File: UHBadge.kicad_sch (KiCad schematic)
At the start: 77 parts, among them J1 Conn_01x03_MountingPin, P1 USB_C_Plug_USB2.0, Q1 Si1308EDL, SW1 Boot, SW2 Run, U1 RP2350A, U2 MCP73871, U3 W25Q128JVS, U4 SRV05-4, U5 Conn, U6 ST25DV64K-JFR6D3, Y1 12MHz

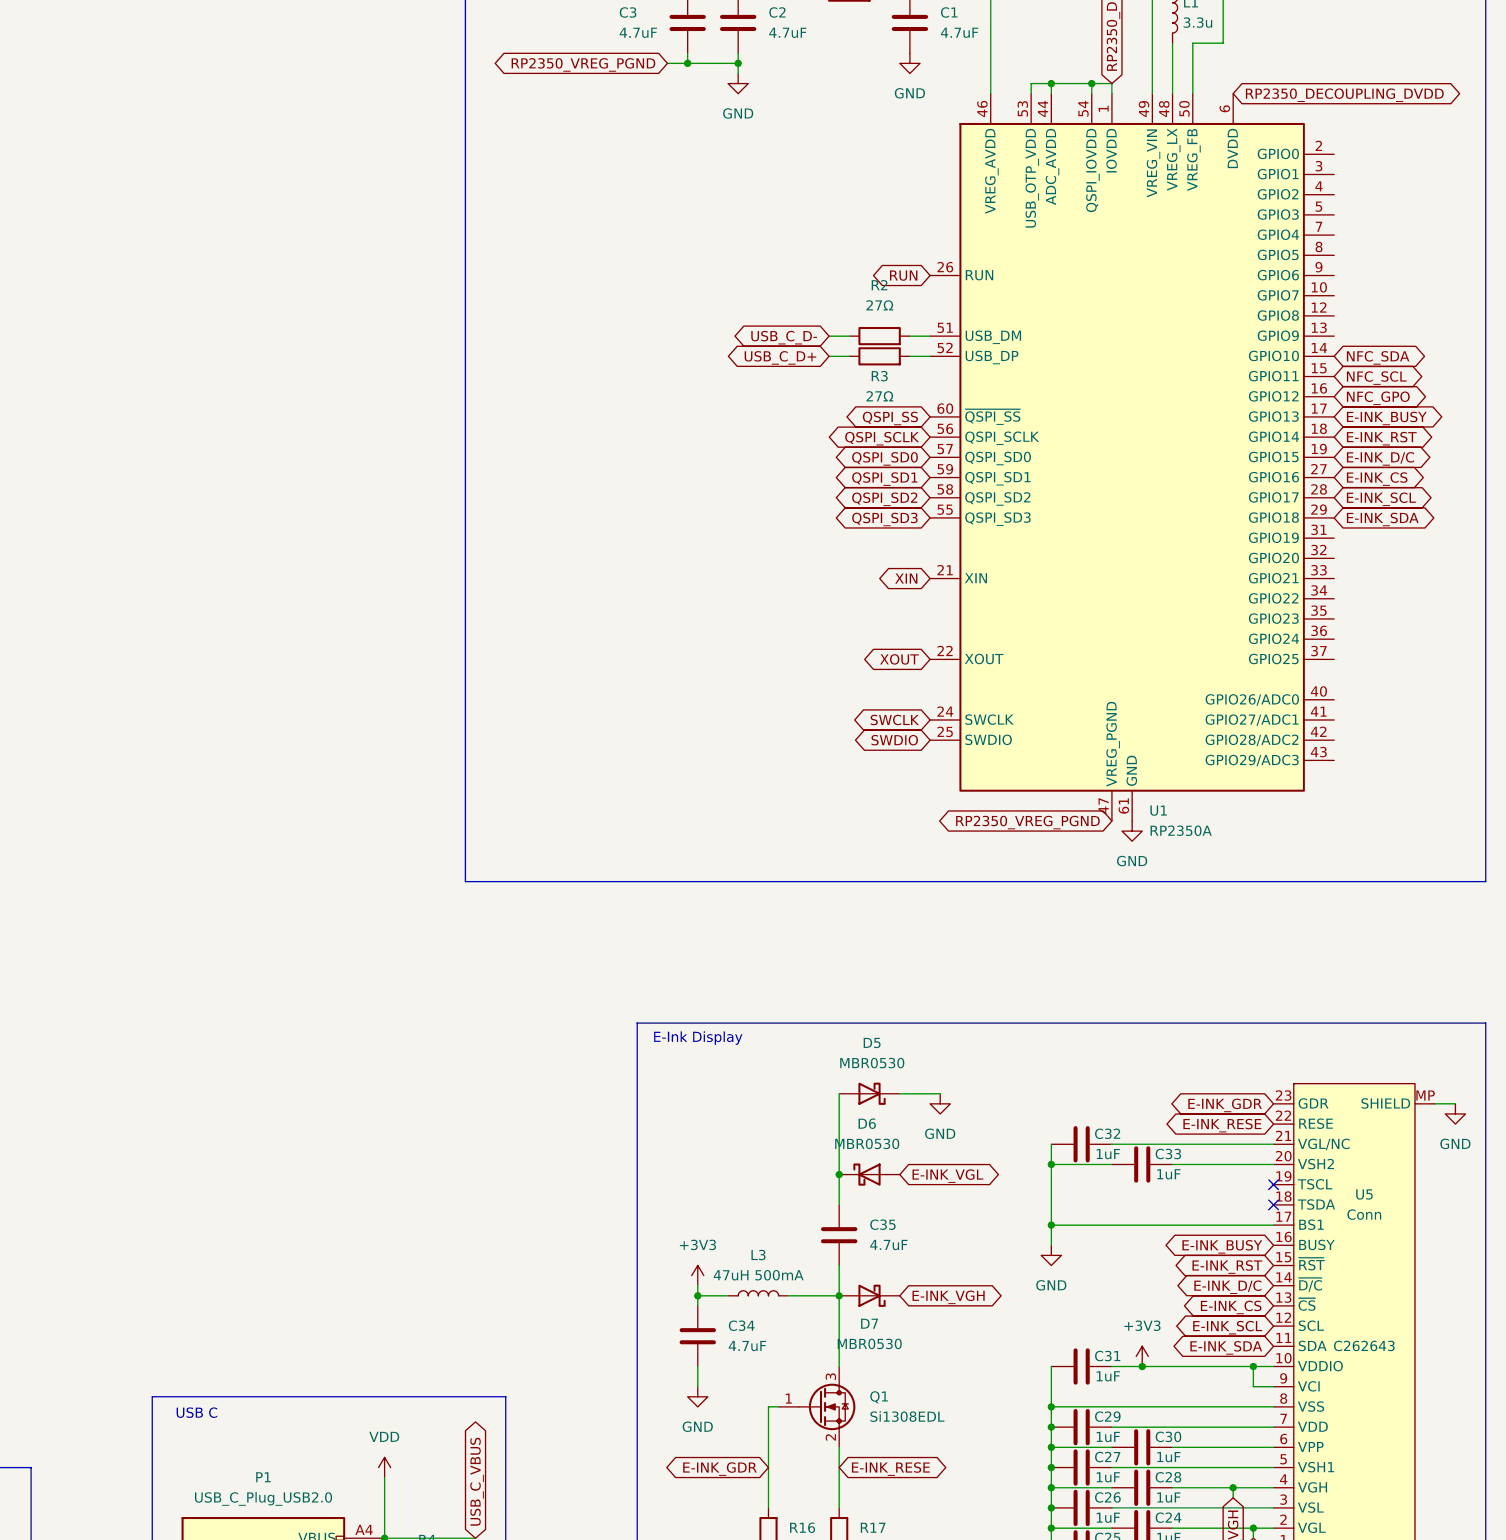
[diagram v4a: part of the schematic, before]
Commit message: Added RP2350 expansion GPIO pins.
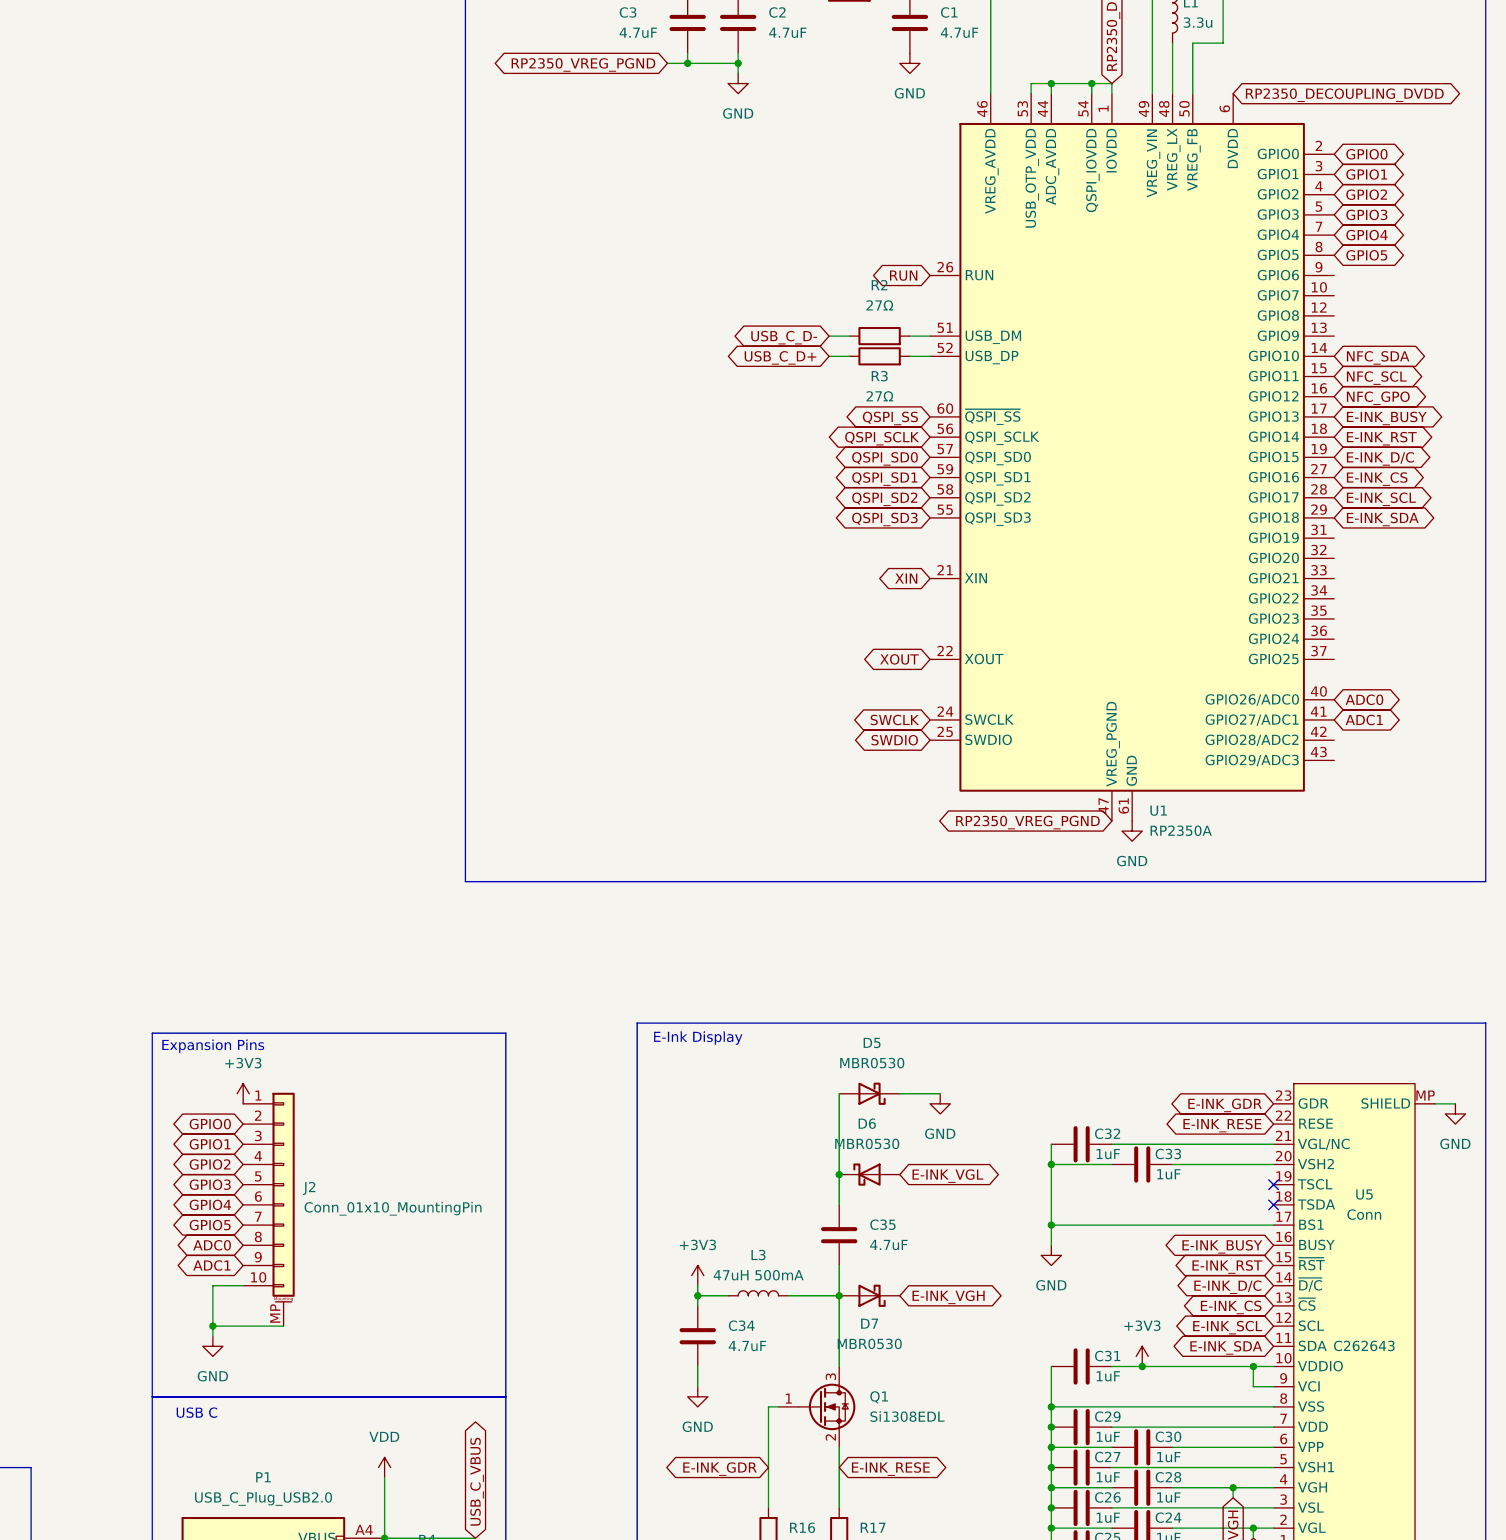
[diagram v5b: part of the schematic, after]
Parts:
- added J2: Conn_01x10_MountingPin, symbol Connector_Generic_MountingPin:Conn_01x10_MountingPin
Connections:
- net +3V3: now also J2.1 (Pin_1)
- net -BATT: now also J2.10 (Pin_10), J2.MP (MountPin)
- net GPIO0: now reaches U1.2 (GPIO0)
- net GPIO0: now also J2.2 (Pin_2)
- net GPIO1: now reaches U1.3 (GPIO1)
- net GPIO1: now also J2.3 (Pin_3)
- net GPIO2: now reaches U1.4 (GPIO2)
- net GPIO2: now also J2.4 (Pin_4)
- net ADC0: now reaches U1.40 (GPIO26/ADC0)
- net ADC0: now also J2.8 (Pin_8)
- net ADC1: now reaches U1.41 (GPIO27/ADC1)
- net ADC1: now also J2.9 (Pin_9)
- net GPIO3: now reaches U1.5 (GPIO3)
- net GPIO3: now also J2.5 (Pin_5)
- net GPIO4: now reaches U1.7 (GPIO4)
- net GPIO4: now also J2.6 (Pin_6)
- net GPIO5: now reaches U1.8 (GPIO5)
- net GPIO5: now also J2.7 (Pin_7)
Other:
- note added: "Expansion Pins"

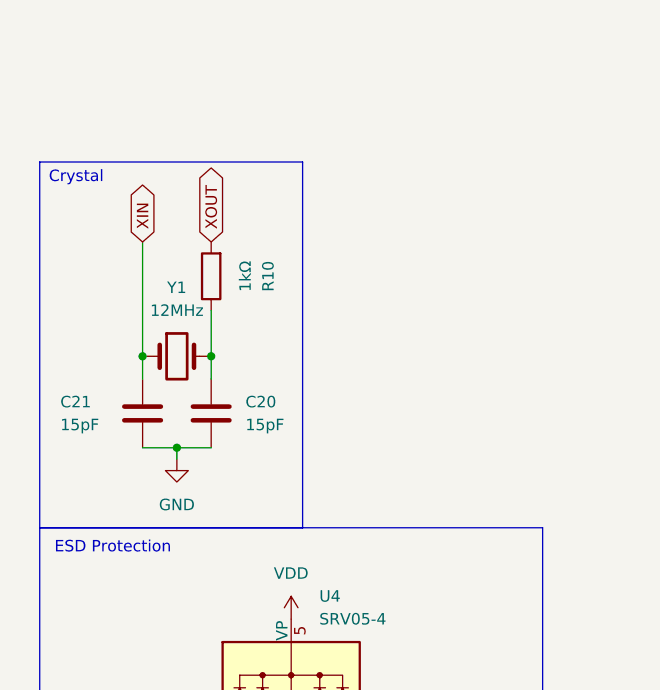
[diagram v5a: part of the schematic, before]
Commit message: Added footprints.
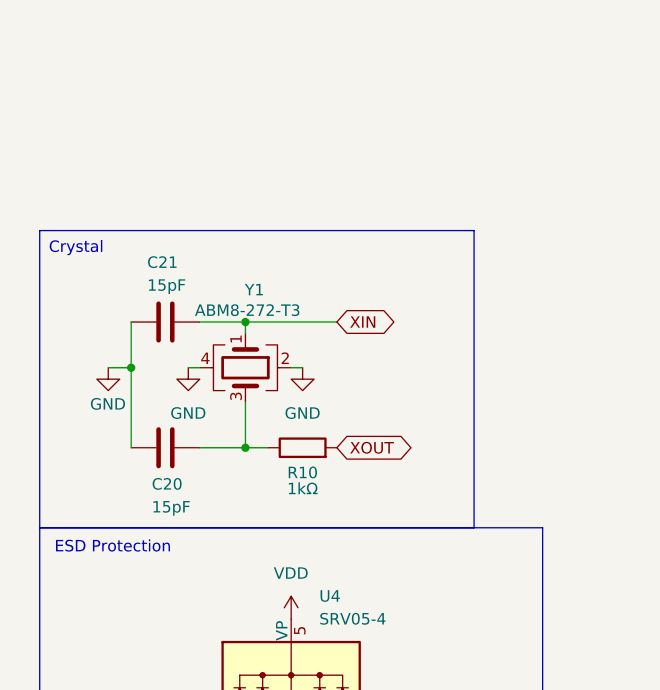
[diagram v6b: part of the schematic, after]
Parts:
- removed Y1: 12MHz, symbol Device:Crystal
- added Y1: ABM8-272-T3, Crystal:Crystal_SMD_3225-4Pin_3.2x2.5mm, symbol Device:Crystal_GND23
- C1, C10, C11, C12, C13, C14, C15, C16, C17, C18, C19, C2, C20, C21, C22, C23, C24, C25, C26, C27, C28, C29, C3, C30, C31, C32, C33, C34, C35, C4, C5, C6, C7, C8, C9: footprint (none) -> Capacitor_SMD:C_0402_1005Metric
- D1, D2, D3, D4: footprint (none) -> LED_SMD:LED_0805_2012Metric
- H1, H2: footprint (none) -> MountingHole:MountingHole_2.2mm_M2_Pad_Via
- J1: footprint (none) -> Connector_PinHeader_1.00mm:PinHeader_1x03_P1.00mm_Vertical
- J2: footprint (none) -> Connector_PinHeader_1.00mm:PinHeader_1x10_P1.00mm_Vertical
- L1: footprint (none) -> CustomFootprints:Inductor
- L2: footprint (none) -> CustomFootprints:NFC_Antenna
- L3: footprint (none) -> Inductor_SMD:L_APV_ANR4018
- P1: footprint (none) -> Connector_USB:USB_C_Receptacle_GCT_USB4105-xx-A_16P_TopMnt_Horizontal
- R1, R10, R11, R12, R13, R14, R15, R16, R17, R2, R3, R4, R5, R6, R7, R8, R9: footprint (none) -> Resistor_SMD:R_0402_1005Metric
- SW1, SW2: footprint (none) -> Button_Switch_THT:SW_PUSH-12mm_Wuerth-430476085716
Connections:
- net -BATT: now also Y1.2, Y1.4
- net XIN: now also Y1.1
- net at C20.1, R10.1: now also Y1.3
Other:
- moved on the sheet: C20, C21, R10

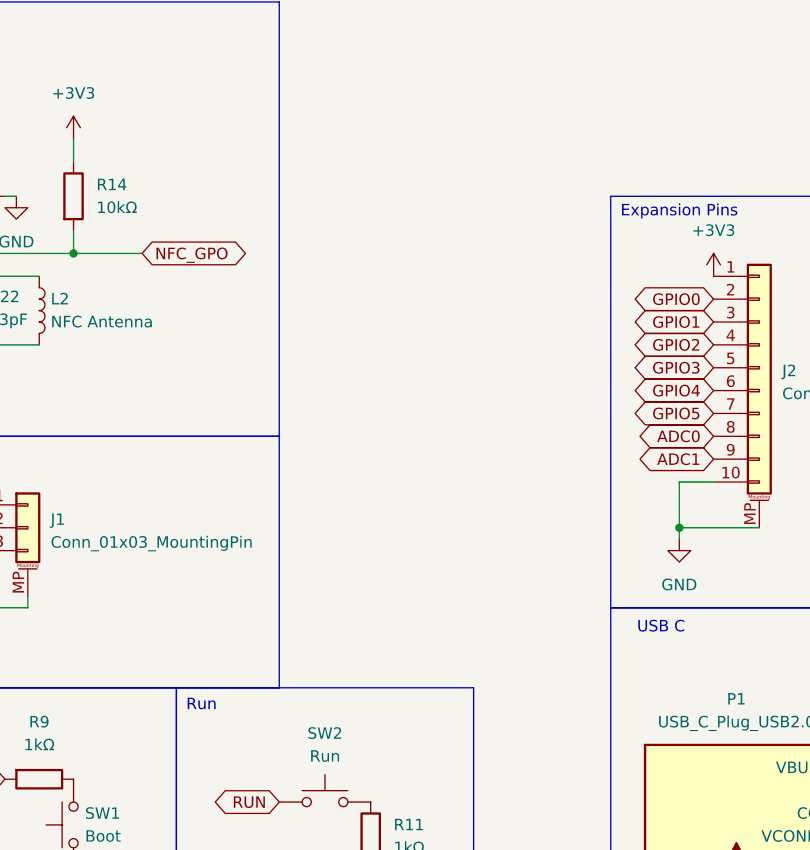
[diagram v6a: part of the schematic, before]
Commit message: Created the Badge borders. Fixed the buttons footprints.
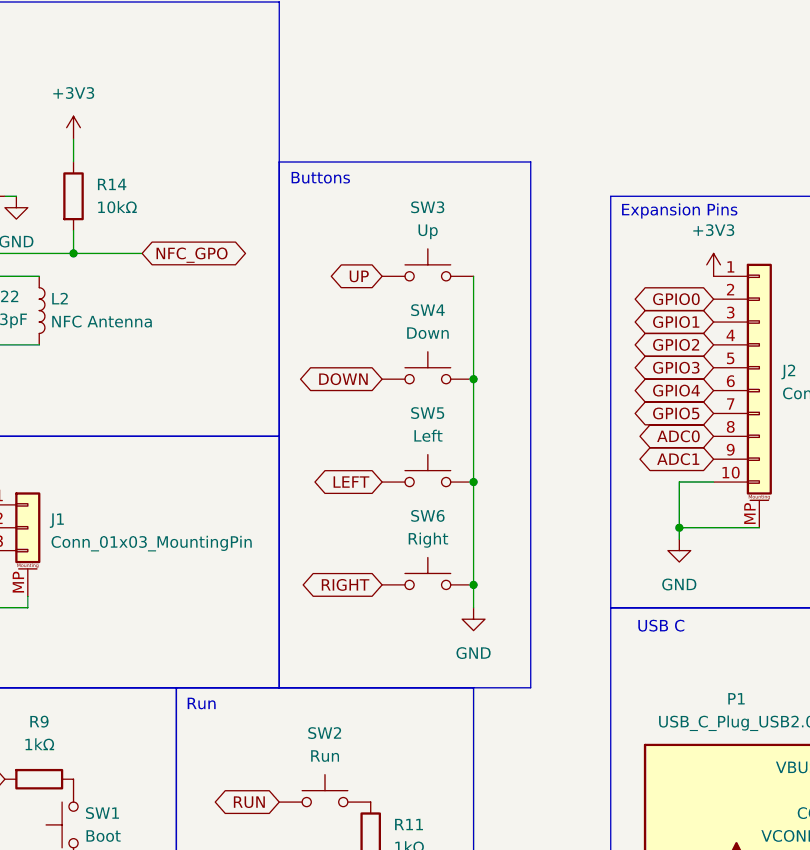
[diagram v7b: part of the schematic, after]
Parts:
- added SW3: Up, Button_Switch_THT:SW_PUSH_6mm, symbol Switch:SW_Push
- added SW4: Down, Button_Switch_THT:SW_PUSH_6mm, symbol Switch:SW_Push
- added SW5: Left, Button_Switch_THT:SW_PUSH_6mm, symbol Switch:SW_Push
- added SW6: Right, Button_Switch_THT:SW_PUSH_6mm, symbol Switch:SW_Push
- SW1, SW2: footprint Button_Switch_THT:SW_PUSH-12mm_Wuerth-430476085716 -> Button_Switch_THT:SW_PUSH_6mm
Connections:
- net -BATT: now also SW3.2, SW4.2, SW5.2, SW6.2
- new net DOWN: SW4.1
- new net LEFT: SW5.1
- new net RIGHT: SW6.1
- new net UP: SW3.1
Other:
- note added: "Buttons"

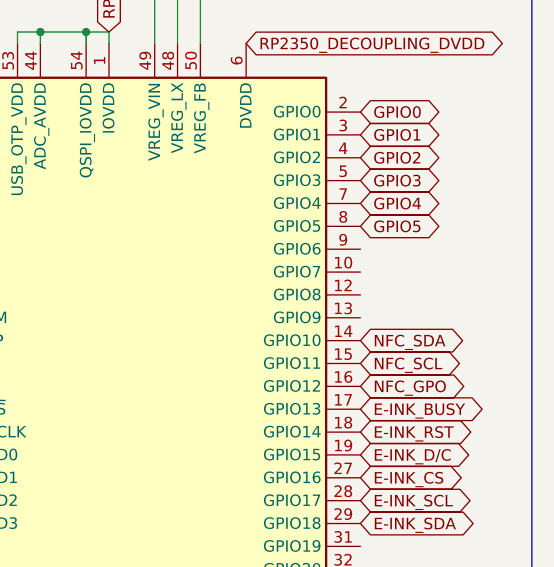
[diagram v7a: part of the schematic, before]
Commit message: Connected the buttons to the RP2350.
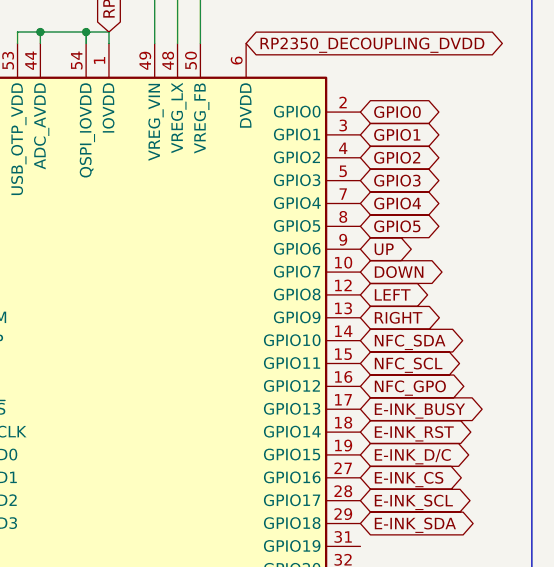
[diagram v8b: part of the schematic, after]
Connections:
- net DOWN: now also U1.10 (GPIO7)
- net LEFT: now also U1.12 (GPIO8)
- net RIGHT: now also U1.13 (GPIO9)
- net UP: now also U1.9 (GPIO6)
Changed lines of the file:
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@@
+		)
+	)
+	(global_label "LEFT"
+		(shape bidirectional)
+		(at 386.08 80.01 0)
+		(fields_autoplaced yes)
+		(effects
+			(font
+				(size 1.27 1.27)
+			)
+			(justify left)
+		)
+		(property "Intersheetrefs" "${INTERSHEET_REFS}"
+			(at 394.4098 80.01 0)
+			(hide yes)
+			(show_name no)
+			(do_not_autoplace no)
+			(effects
+				(font
+					(size 1.27 1.27)
+				)
+				(justify left)
+			)
 		)
 	)
@@
 		)
 	)
+	(global_label "RIGHT"
+		(shape bidirectional)
+		(at 386.08 82.55 0)
+		(fields_autoplaced yes)
+		(effects
+			(font
+				(size 1.27 1.27)
+			)
+			(justify left)
+		)
+		(property "Intersheetrefs" "${INTERSHEET_REFS}"
+			(at 395.6194 82.55 0)
+			(hide yes)
+			(show_name no)
+			(do_not_autoplace no)
+			(effects
+				(font
+					(size 1.27 1.27)
+				)
+				(justify left)
+			)
+		)
+	)
 	(global_label "GPIO3"
 		(shape bidirectional)
@@
 		)
 	)
+	(global_label "DOWN"
+		(shape bidirectional)
+		(at 386.08 77.47 0)
+		(fields_autoplaced yes)
+		(effects
+			(font
+				(size 1.27 1.27)
+			)
+			(justify left)
+		)
+		(property "Intersheetrefs" "${INTERSHEET_REFS}"
+			(at 395.5589 77.47 0)
+			(hide yes)
+			(show_name no)
+			(do_not_autoplace no)
+			(effects
+				(font
+					(size 1.27 1.27)
+				)
+				(justify left)
+			)
+		)
+	)
 	(global_label "RP2350_DECOUPLING_IOVDD+"
 		(shape bidirectional)
@@
 			)
 		)
+	)
+	(global_label "UP"
+		(shape bidirectional)
+		(at 386.08 74.93 0)
+		(fields_autoplaced yes)
+		(effects
+			(font
+				(size 1.27 1.27)
+			)
+			(justify left)
+		)
+		(property "Intersheetrefs" "${INTERSHEET_REFS}"
+			(at 392.777 74.93 0)
+			(hide yes)
+			(show_name no)
+			(do_not_autoplace no)
+			(effects
+				(font
+					(size 1.27 1.27)
+				)
+				(justify left)
+			)
+		)
